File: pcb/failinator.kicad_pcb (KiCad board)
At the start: 2 copper layers, 200 x 124 mm, 68 parts, among them P1 CONN_01X04, P2 CONN_01X06, P3 CONN_01X06, P4 CONN_01X06, U1 74HC594, U2 RASPIPLUSHEADER, U3 LDS-CD16RI, U4 LDS-CD16RI, U5 74HC594

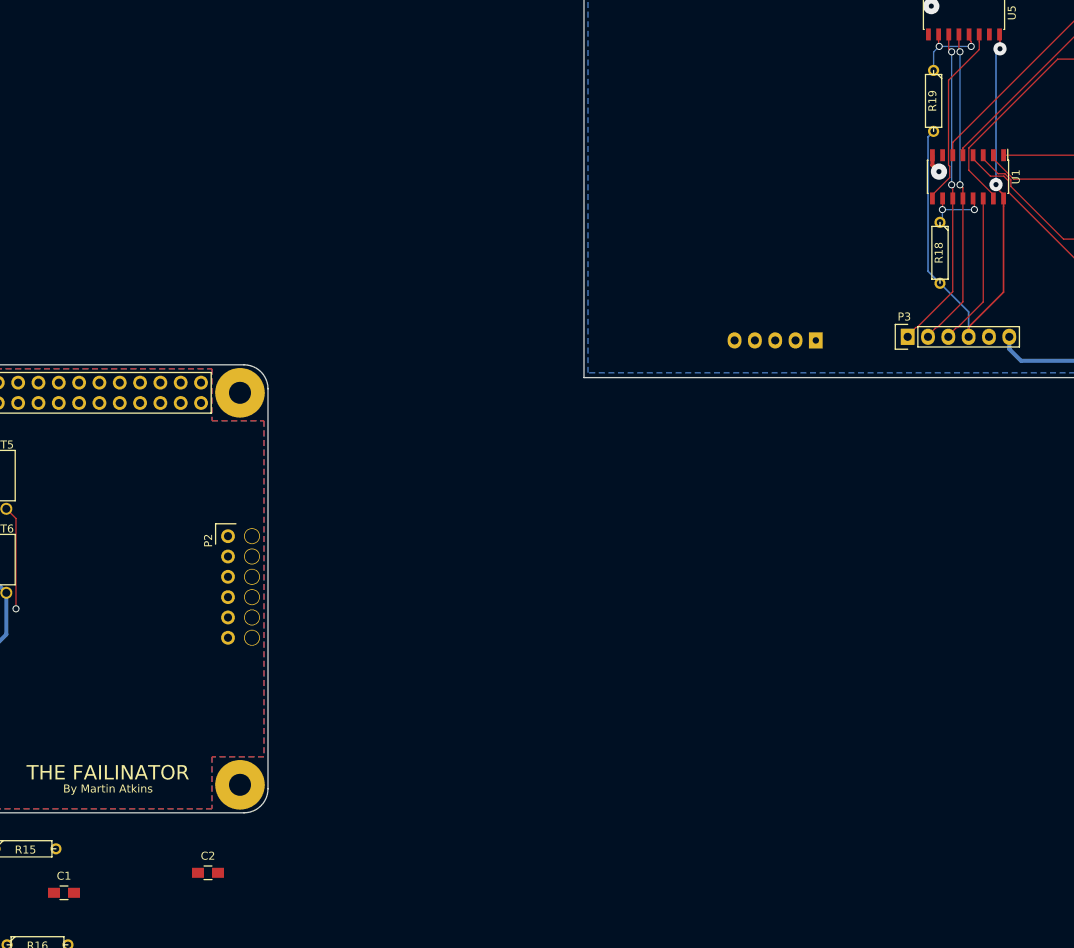
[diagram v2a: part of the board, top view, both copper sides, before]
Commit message: Shift register decoupling capacitors
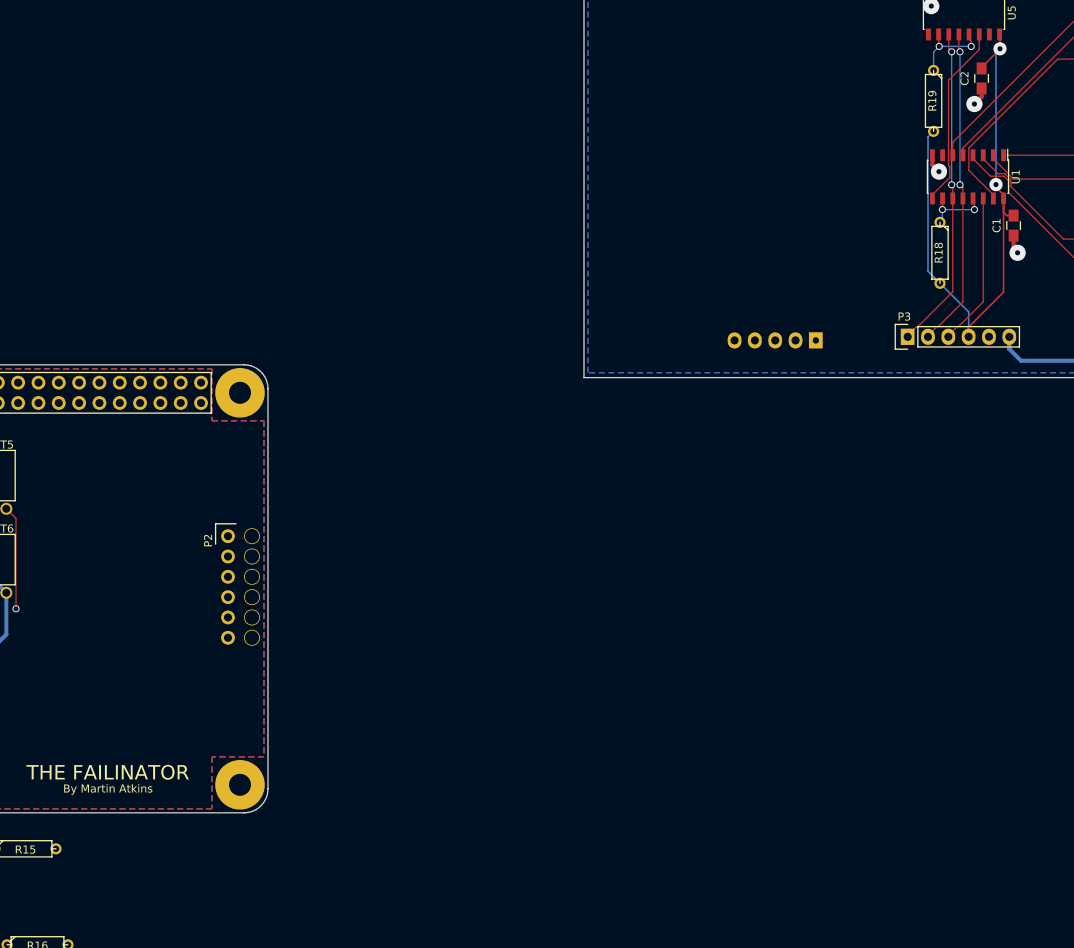
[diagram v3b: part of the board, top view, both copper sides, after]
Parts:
- moved C1 145.1 mm to (253.7, 50.6), turned to 90 degrees
- moved C2 138.6 mm to (249.7, 32.2), turned to 90 degrees
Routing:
- net /D_+3V3: track 68.3 -> 73.9 mm
- net /DisplayDrivers/GND: track 4.41 -> 9.09 mm, vias 2 -> 4
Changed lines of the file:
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@@
     (thickness 1.6)
     (drawings 16)
-    (tracks 319)
+    (tracks 331)
     (zones 0)
     (modules 68)
@@
   )
   (module Capacitors_SMD:C_0805_HandSoldering (layer F.Cu)
-    (at 135 134)
+    (at 253.7 50.6 90)
     (descr "Capacitor SMD 0805, hand soldering")
     (tags "capacitor 0805")
     (attr smd)
-    (fp_text reference C1 (at 0 -2.1) (layer F.SilkS)
-      (effects (font (size 1 1) (thickness 0.15)))
-    )
-    (fp_text value C_Small (at 0 2.1) (layer F.Fab)
+    (fp_text reference C1 (at 0 -2.1 90) (layer F.SilkS)
+      (effects (font (size 1 1) (thickness 0.15)))
+    )
+    (fp_text value C_Small (at 0 2.1 90) (layer F.Fab)
       (effects (font (size 1 1) (thickness 0.15)))
     )
@@
     (fp_line (start 0.5 -0.85) (end -0.5 -0.85) (layer F.SilkS) (width 0.15))
     (fp_line (start -0.5 0.85) (end 0.5 0.85) (layer F.SilkS) (width 0.15))
-    (pad 1 smd rect (at -1.25 0) (size 1.5 1.25) (layers F.Cu F.Paste F.Mask)
-      (net 38 /DisplayDrivers/GND))
-    (pad 2 smd rect (at 1.25 0) (size 1.5 1.25) (layers F.Cu F.Paste F.Mask)
+    (pad 1 smd rect (at -1.25 0 90) (size 1.5 1.25) (layers F.Cu F.Paste F.Mask)
+      (net 38 /DisplayDrivers/GND))
+    (pad 2 smd rect (at 1.25 0 90) (size 1.5 1.25) (layers F.Cu F.Paste F.Mask)
       (net 39 /D_+3V3))
     (model Capacitors_SMD.3dshapes/C_0805_HandSoldering.wrl
@@
   )
   (module Capacitors_SMD:C_0805_HandSoldering (layer F.Cu)
-    (at 153 131.5)
+    (at 249.7 32.2 90)
     (descr "Capacitor SMD 0805, hand soldering")
     (tags "capacitor 0805")
     (attr smd)
-    (fp_text reference C2 (at 0 -2.1) (layer F.SilkS)
-      (effects (font (size 1 1) (thickness 0.15)))
-    )
-    (fp_text value C_Small (at 0 2.1) (layer F.Fab)
+    (fp_text reference C2 (at 0 -2.1 90) (layer F.SilkS)
+      (effects (font (size 1 1) (thickness 0.15)))
+    )
+    (fp_text value C_Small (at 0 2.1 90) (layer F.Fab)
       (effects (font (size 1 1) (thickness 0.15)))
     )
@@
     (fp_line (start 0.5 -0.85) (end -0.5 -0.85) (layer F.SilkS) (width 0.15))
     (fp_line (start -0.5 0.85) (end 0.5 0.85) (layer F.SilkS) (width 0.15))
-    (pad 1 smd rect (at -1.25 0) (size 1.5 1.25) (layers F.Cu F.Paste F.Mask)
-      (net 38 /DisplayDrivers/GND))
-    (pad 2 smd rect (at 1.25 0) (size 1.5 1.25) (layers F.Cu F.Paste F.Mask)
+    (pad 1 smd rect (at -1.25 0 90) (size 1.5 1.25) (layers F.Cu F.Paste F.Mask)
+      (net 38 /DisplayDrivers/GND))
+    (pad 2 smd rect (at 1.25 0 90) (size 1.5 1.25) (layers F.Cu F.Paste F.Mask)
       (net 39 /D_+3V3))
     (model Capacitors_SMD.3dshapes/C_0805_HandSoldering.wrl
@@
   (segment (start 125.5 96.5) (end 125.5 118.75) (width 0.508) (layer F.Cu) (net 37) (status 10))
   (segment (start 125.5 118.75) (end 124.25 120) (width 0.508) (layer F.Cu) (net 37) (status 20))
+  (segment (start 249.7 33.45) (end 249.7 34.5) (width 0.508) (layer F.Cu) (net 38))
+  (segment (start 249.7 34.5) (end 248.8 35.4) (width 0.508) (layer F.Cu) (net 38))
+  (via (at 248.8 35.4) (size 2.032) (drill 0.635) (layers F.Cu B.Cu) (net 38))
+  (segment (start 253.7 51.85) (end 253.7 53.5) (width 0.508) (layer F.Cu) (net 38))
+  (segment (start 253.7 53.5) (end 254.2 54) (width 0.508) (layer F.Cu) (net 38))
+  (via (at 254.2 54) (size 2.032) (drill 0.635) (layers F.Cu B.Cu) (net 38))
   (segment (start 244.346901 43.849901) (end 244.373121 43.849901) (width 0.508) (layer F.Cu) (net 38))
   (segment (start 243.555 43.058) (end 244.346901 43.849901) (width 0.508) (layer F.Cu) (net 38))
@@
   (segment (start 243.055 22.805841) (end 243.410718 23.161559) (width 0.508) (layer F.Cu) (net 38))
   (via (at 243.410718 23.161559) (size 2.032) (drill 0.635) (layers F.Cu B.Cu) (net 38))
+  (segment (start 249.7 30.95) (end 249.7 30.825) (width 0.2032) (layer F.Cu) (net 39))
+  (segment (start 249.7 30.825) (end 252 28.525) (width 0.2032) (layer F.Cu) (net 39))
+  (segment (start 252 28.525) (end 252 28.5) (width 0.2032) (layer F.Cu) (net 39))
+  (segment (start 253.7 49.35) (end 252.8718 49.35) (width 0.2032) (layer F.Cu) (net 39))
+  (segment (start 252.8718 49.35) (end 252.445 48.9232) (width 0.2032) (layer F.Cu) (net 39))
+  (segment (start 252.445 48.9232) (end 252.445 48.1532) (width 0.2032) (layer F.Cu) (net 39))
+  (segment (start 252.445 48.1532) (end 252.445 47.2) (width 0.2032) (layer F.Cu) (net 39))
   (segment (start 243.001501 56.311501) (end 243.801501 57.111501) (width 0.2032) (layer B.Cu) (net 39))
   (segment (start 243.801501 57.111501) (end 244.5 57.81) (width 0.2032) (layer B.Cu) (net 39))
@@
   (segment (start 248.08 63.2808) (end 252.445 58.9158) (width 0.2032) (layer F.Cu) (net 39))
   (segment (start 252.445 58.9158) (end 252.445 48.1532) (width 0.2032) (layer F.Cu) (net 39))
-  (segment (start 252.445 48.1532) (end 252.445 47.2) (width 0.2032) (layer F.Cu) (net 39))
   (segment (start 270.43934 29.79) (end 271.5 29.79) (width 0.1524) (layer F.Cu) (net 40))
   (segment (start 248.106399 43.681399) (end 248.106399 40.893601) (width 0.1524) (layer F.Cu) (net 40))

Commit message: Main board traces to the display board connector
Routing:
- net +3V3: track 22.8 -> 64.9 mm
- net /MOSI: track 0.14 -> 38.6 mm
- net /DISP_CS: track 0.01 -> 36.5 mm
- net /SCLK: track 0.00 -> 31.3 mm
- net +24V: track 75.4 -> 105.4 mm
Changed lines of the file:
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@@
     (thickness 1.6)
     (drawings 16)
-    (tracks 331)
+    (tracks 355)
     (zones 0)
     (modules 68)
@@
   (segment (start 107.5 86) (end 105.21 88.29) (width 0.1524) (layer F.Cu) (net 3) (status 10))
   (segment (start 105.21 88.29) (end 105.21 96.5) (width 0.1524) (layer F.Cu) (net 3) (status 20))
+  (segment (start 127.79 96.5) (end 149.88 96.5) (width 0.508) (layer B.Cu) (net 4))
+  (segment (start 149.88 96.5) (end 155.5 102.12) (width 0.508) (layer B.Cu) (net 4))
   (segment (start 123 106.5) (end 127.79 101.71) (width 0.508) (layer B.Cu) (net 4) (status 10))
   (segment (start 127.79 101.71) (end 127.79 96.5) (width 0.508) (layer B.Cu) (net 4) (status 20))
@@
   (segment (start 125.5 86) (end 125.5 94.21) (width 0.1524) (layer F.Cu) (net 6) (status 10))
   (segment (start 125.5 94.21) (end 123.21 96.5) (width 0.1524) (layer F.Cu) (net 6) (status 20))
+  (segment (start 126.73 72.77) (end 126.73 73.991314) (width 0.1524) (layer F.Cu) (net 7))
+  (segment (start 126.73 73.991314) (end 147.238686 94.5) (width 0.1524) (layer F.Cu) (net 7))
+  (segment (start 147.238686 94.5) (end 154.278686 94.5) (width 0.1524) (layer F.Cu) (net 7))
+  (segment (start 154.278686 94.5) (end 155.5 94.5) (width 0.1524) (layer F.Cu) (net 7))
   (segment (start 126.73 72.77) (end 126.872 72.77) (width 0.1524) (layer F.Cu) (net 7) (status 30))
+  (segment (start 131.81 70.23) (end 132.902201 71.322201) (width 0.1524) (layer F.Cu) (net 8))
+  (segment (start 132.902201 71.322201) (end 134.518659 71.322201) (width 0.1524) (layer F.Cu) (net 8))
+  (segment (start 134.518659 71.322201) (end 135.797799 72.601341) (width 0.1524) (layer F.Cu) (net 8))
+  (segment (start 135.797799 72.601341) (end 135.797799 73.294257) (width 0.1524) (layer F.Cu) (net 8))
+  (segment (start 135.797799 73.294257) (end 150.831341 88.327799) (width 0.1524) (layer F.Cu) (net 8))
+  (segment (start 150.831341 88.327799) (end 156.024257 88.327799) (width 0.1524) (layer F.Cu) (net 8))
+  (segment (start 156.592201 90.867799) (end 156.363599 91.096401) (width 0.1524) (layer F.Cu) (net 8))
+  (segment (start 156.024257 88.327799) (end 156.592201 88.895743) (width 0.1524) (layer F.Cu) (net 8))
+  (segment (start 156.592201 88.895743) (end 156.592201 90.867799) (width 0.1524) (layer F.Cu) (net 8))
+  (segment (start 156.363599 91.096401) (end 155.5 91.96) (width 0.1524) (layer F.Cu) (net 8))
   (segment (start 131.81 70.23) (end 131.81 70.244) (width 0.1524) (layer F.Cu) (net 8) (status 30))
+  (segment (start 131.81 72.77) (end 131.81 73.991314) (width 0.1524) (layer F.Cu) (net 9))
+  (segment (start 131.81 73.991314) (end 147.238686 89.42) (width 0.1524) (layer F.Cu) (net 9))
+  (segment (start 147.238686 89.42) (end 154.278686 89.42) (width 0.1524) (layer F.Cu) (net 9))
+  (segment (start 154.278686 89.42) (end 155.5 89.42) (width 0.1524) (layer F.Cu) (net 9))
+  (segment (start 124.19 72.77) (end 124.19 73.991314) (width 0.2032) (layer F.Cu) (net 10))
+  (segment (start 124.19 73.991314) (end 147.238686 97.04) (width 0.2032) (layer F.Cu) (net 10))
+  (segment (start 147.238686 97.04) (end 154.278686 97.04) (width 0.2032) (layer F.Cu) (net 10))
+  (segment (start 154.278686 97.04) (end 155.5 97.04) (width 0.2032) (layer F.Cu) (net 10))
   (segment (start 103.87 72.77) (end 104.012 72.77) (width 0.1524) (layer B.Cu) (net 10) (status 30))
   (segment (start 124.19 72.77) (end 124.586 72.77) (width 0.1524) (layer B.Cu) (net 10) (status 30))

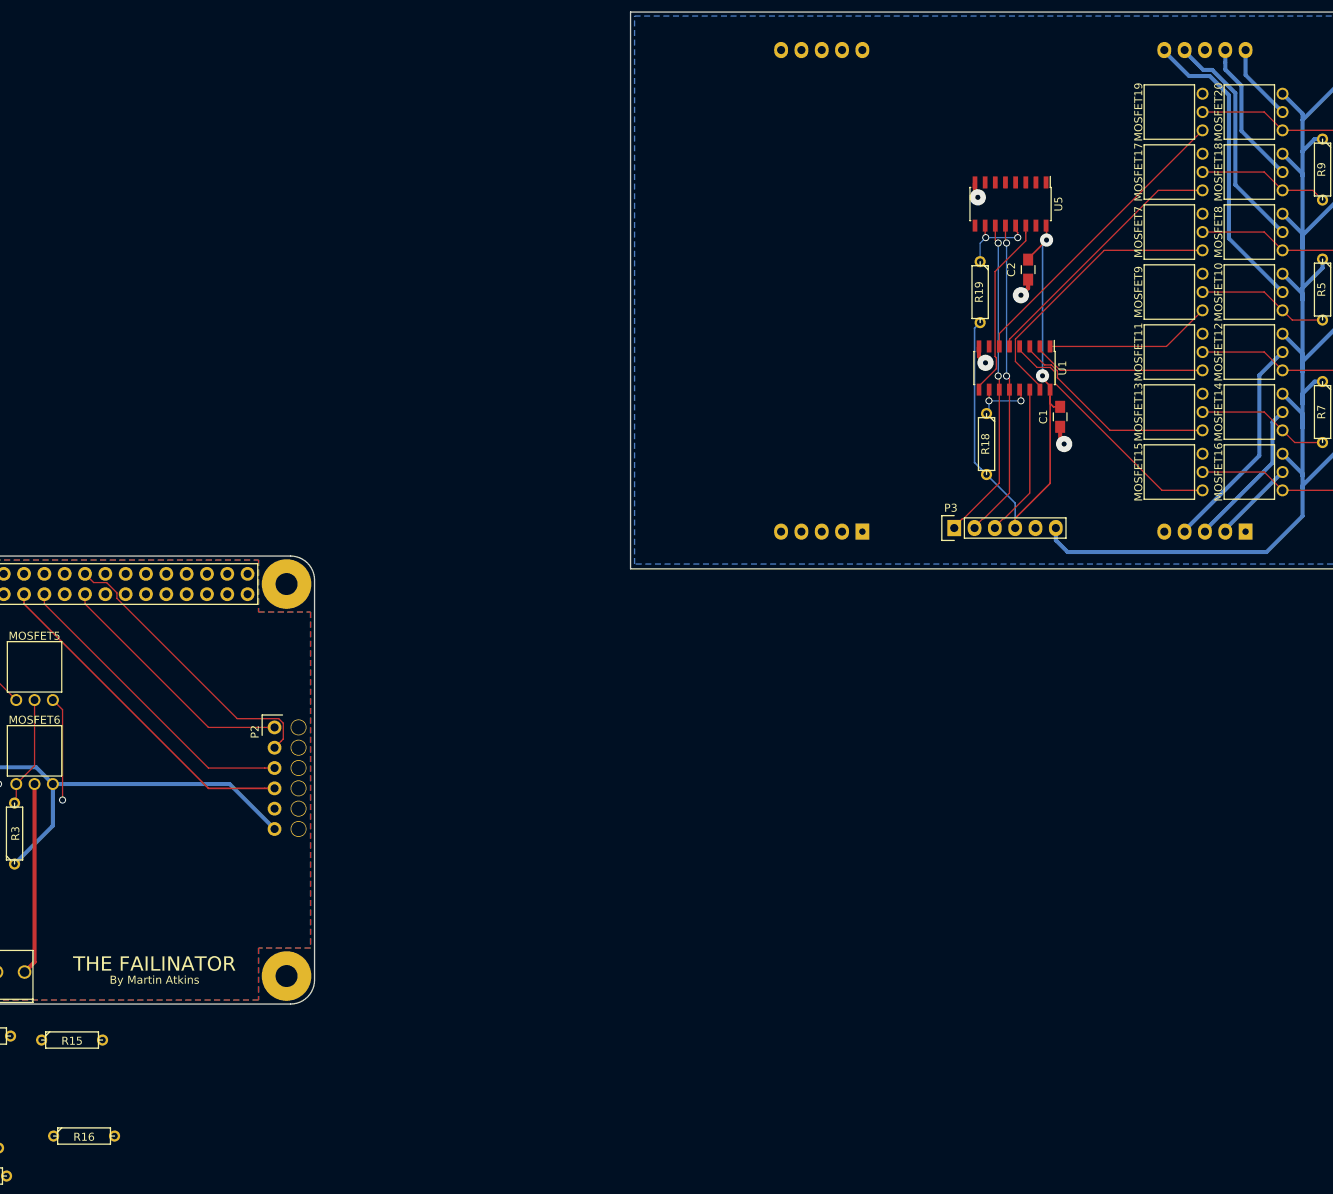
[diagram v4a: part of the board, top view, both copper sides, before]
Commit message: Rework digit 0 layout for current-limiting resistors
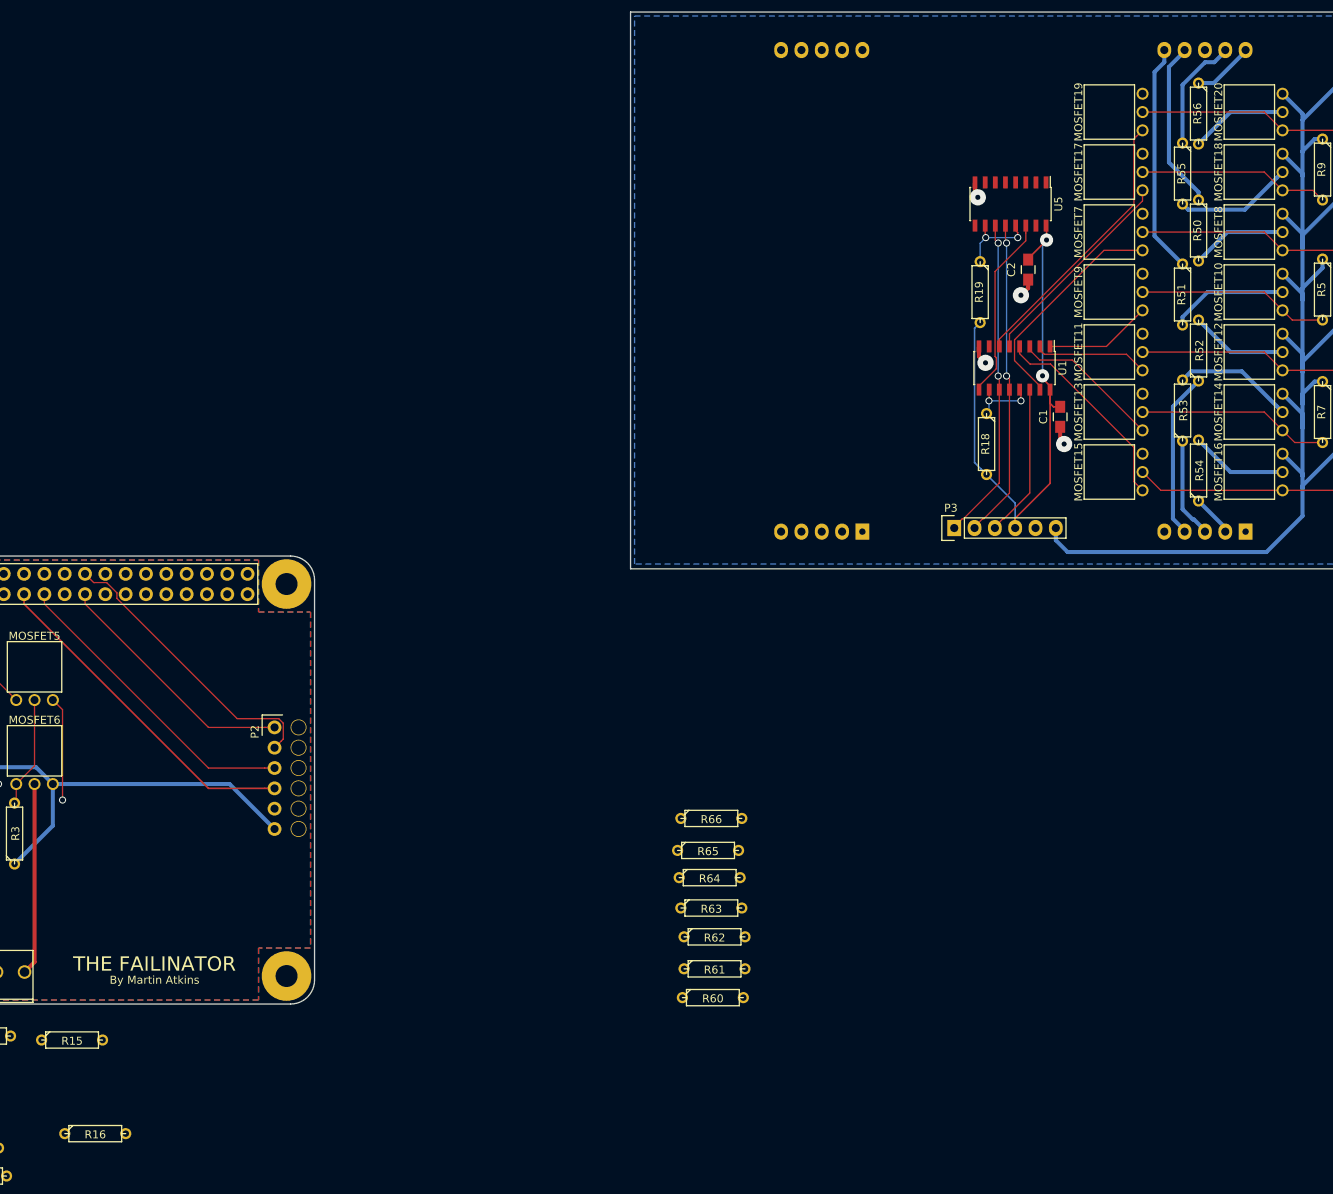
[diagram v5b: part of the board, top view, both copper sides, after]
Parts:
- added R50: 150, Discret:R3, F.Cu at (271.0, 27.3)
- added R51: 150, Discret:R3, F.Cu at (269.0, 35.3)
- added R52: 150, Discret:R3, F.Cu at (271.0, 42.3)
- added R53: 150, Discret:R3, F.Cu at (269.0, 49.8)
- added R54: 150, Discret:R3, F.Cu at (271.0, 57.3)
- added R55: 150, Discret:R3, F.Cu at (269.0, 20.2)
- added R56: 150, Discret:R3, F.Cu at (271.0, 12.7)
- added R60: 150, Discret:R3, F.Cu at (210.3, 123.2)
- added R61: 150, Discret:R3, F.Cu at (210.5, 119.6)
- added R62: 150, Discret:R3, F.Cu at (210.5, 115.6)
- added R63: 150, Discret:R3, F.Cu at (210.1, 112.0)
- added R64: 150, Discret:R3, F.Cu at (209.9, 108.2)
- added R65: 150, Discret:R3, F.Cu at (209.7, 104.8)
- added R66: 150, Discret:R3, F.Cu at (210.1, 100.8)
- moved MOSFET11 7.50 mm to (264.0, 42.5)
- moved MOSFET13 7.50 mm to (264.0, 50.0)
- moved MOSFET15 7.50 mm to (264.0, 57.5)
- moved MOSFET17 7.50 mm to (264.0, 20.0)
- moved MOSFET19 7.50 mm to (264.0, 12.5)
- moved MOSFET7 7.50 mm to (264.0, 27.5)
- moved MOSFET9 7.50 mm to (264.0, 35.0)
- moved R16 1.43 mm to (133.1, 140.2)
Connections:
- MOSFET10 pad 2: /DisplayDrivers/B0_P -> /DisplayDrivers/B0Driver/VOUT
- MOSFET12 pad 2: /DisplayDrivers/C0_P -> /DisplayDrivers/C0Driver/VOUT
- MOSFET14 pad 2: /DisplayDrivers/D0_P -> /DisplayDrivers/D0Driver/VOUT
- MOSFET16 pad 2: /DisplayDrivers/E0_P -> /DisplayDrivers/E0Driver/VOUT
- MOSFET18 pad 2: /DisplayDrivers/F0_P -> /DisplayDrivers/F0Driver/VOUT
- MOSFET20 pad 2: /DisplayDrivers/G0_P -> /DisplayDrivers/G0Driver/VOUT
- MOSFET22 pad 2: /DisplayDrivers/A1_P -> /DisplayDrivers/A1Driver/VOUT
- MOSFET24 pad 2: /DisplayDrivers/B1_P -> /DisplayDrivers/B1Driver/VOUT
- MOSFET26 pad 2: /DisplayDrivers/C1_P -> /DisplayDrivers/C1Driver/VOUT
- MOSFET28 pad 2: /DisplayDrivers/D1_P -> /DisplayDrivers/D1Driver/VOUT
- MOSFET30 pad 2: /DisplayDrivers/E1_P -> /DisplayDrivers/E1Driver/VOUT
- MOSFET32 pad 2: /DisplayDrivers/F1_P -> /DisplayDrivers/F1Driver/VOUT
- MOSFET34 pad 2: /DisplayDrivers/G1_P -> /DisplayDrivers/G1Driver/VOUT
- MOSFET8 pad 2: /DisplayDrivers/A0_P -> /DisplayDrivers/A0Driver/VOUT
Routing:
- net /DisplayDrivers/D0Driver/VOUT: track 0.00 -> 15.1 mm
- net /DisplayDrivers/B0Driver/VOUT: track 0.00 -> 14.8 mm
- net /DisplayDrivers/F0Driver/VOUT: track 0.00 -> 14.7 mm
- net /DisplayDrivers/G0Driver/VOUT: track 0.00 -> 12.2 mm
- net /DisplayDrivers/E0Driver/VOUT: track 0.00 -> 12.2 mm
- net /DisplayDrivers/C0Driver/VOUT: track 0.00 -> 12.2 mm
- net /DisplayDrivers/A0Driver/VOUT: track 0.00 -> 12.0 mm
- net /DisplayDrivers/B0_P: track 37.9 -> 28.7 mm
- net /DisplayDrivers/D0_L: track 26.7 -> 18.7 mm
- net Net-(MOSFET7-Pad2): track 19.4 -> 26.9 mm
- net Net-(MOSFET17-Pad2): track 16.4 -> 23.9 mm
- net Net-(MOSFET11-Pad2): track 19.4 -> 26.9 mm
- net Net-(MOSFET10-Pad1): track 16.4 -> 23.9 mm
- net /DisplayDrivers/B0_L: track 20.9 -> 13.4 mm
- net Net-(MOSFET19-Pad2): track 19.3 -> 26.8 mm
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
